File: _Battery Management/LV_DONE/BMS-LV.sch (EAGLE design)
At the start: 120 parts, among them J1 M1x5, J2 M1x4, J3 M1x4, J4 M1x4, J5 M1x2, J6 MX150L, J7 M2770166, J8 M1x5, J9 M80022232081-2, K1 ADJ14024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

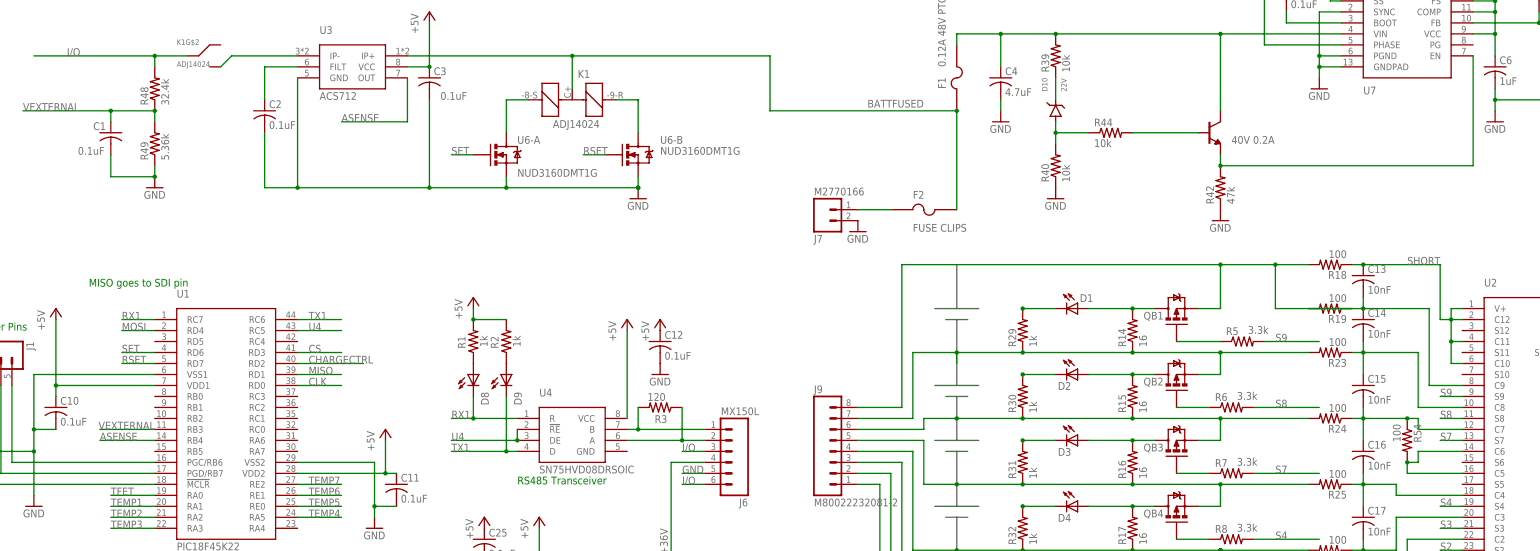
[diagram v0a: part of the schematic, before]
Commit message: 
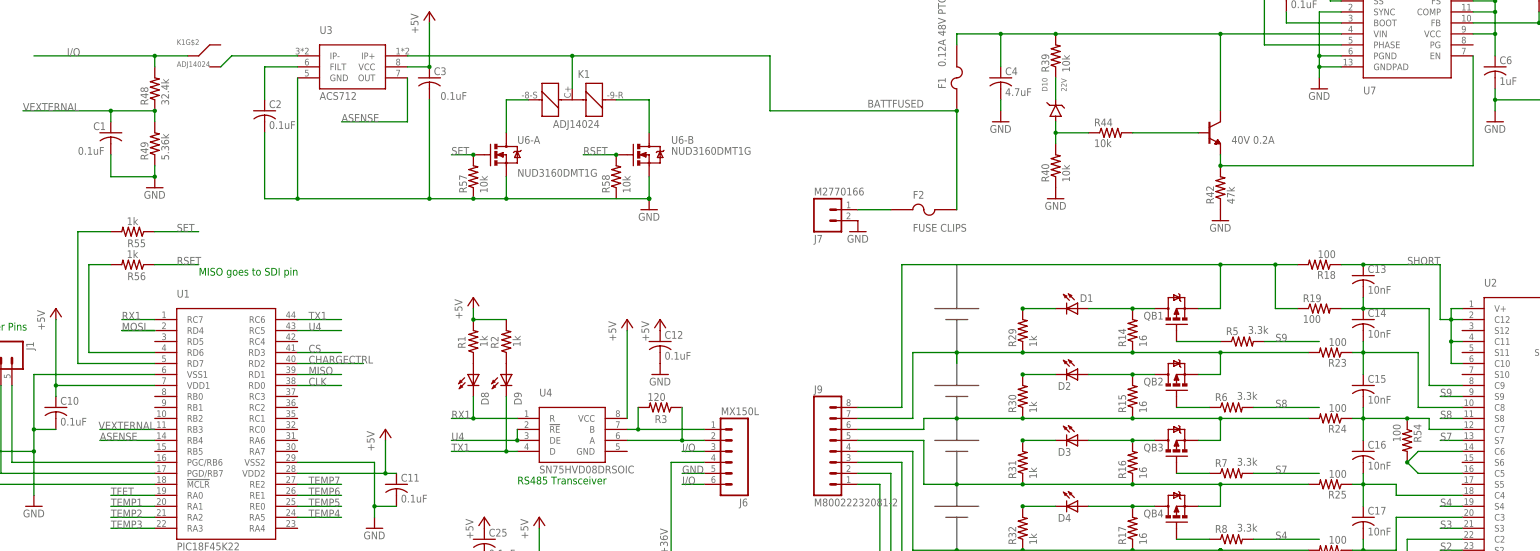
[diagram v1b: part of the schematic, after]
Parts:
- added R55, R56: 1k, FSAE Electric:RES_1K_5%
- added R57, R58: 10k, FSAE Electric:RES_10K_1%
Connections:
- new net N$19: R56.2, U1.RD6
- new net N$6: R55.2, U1.RD7
- net GND: now also R57.1
- net RSET: now also R58.2; no longer U1.RD7
- net SET: now also R55.1, R57.2; no longer U1.RD6
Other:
- moved on the sheet: R18, R19, U6-B

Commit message: 
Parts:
- removed C24: 10uF, FSAE Electric:CAP_10UF_50V
- removed C25, C26: 0.1uF, FSAE Electric:CAP_0.1UF_50V
- removed Q3: BDX34C, FSAE Electric:PNP_BDX34C
- removed R36: 1k, FSAE Electric:RES_1K_5%
- removed R38: 0.5, FSAE Electric:RES_0.5_5%_CHASSISMNT
- removed R53: 100, FSAE Electric:RES_100_1%
- removed U9: OPA344, FSAE Electric:OPA344
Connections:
- removed net +36V: J6.4, Q3.E
- removed net CHARGECTRL: R36.1, U1.RD2
- removed net N$14: C24.+, R36.2, U9.+
- removed net N$17: Q3.B, R53.2
- removed net N$21: C26.+, R53.1, U9.O
- removed net N$23: C26.-, Q3.C, R38.2, U9.-
- removed net VREG: C23.+, R47.2
- net +5V: now also C23.+, R47.2; no longer C25.+, U9.V+
- net BATTFUSED: no longer R38.1
- net GND: now also J6.2; no longer C24.-, C25.-, U9.V-
- net N$29: now also J6.4; no longer J6.2
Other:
- moved on the sheet: J6

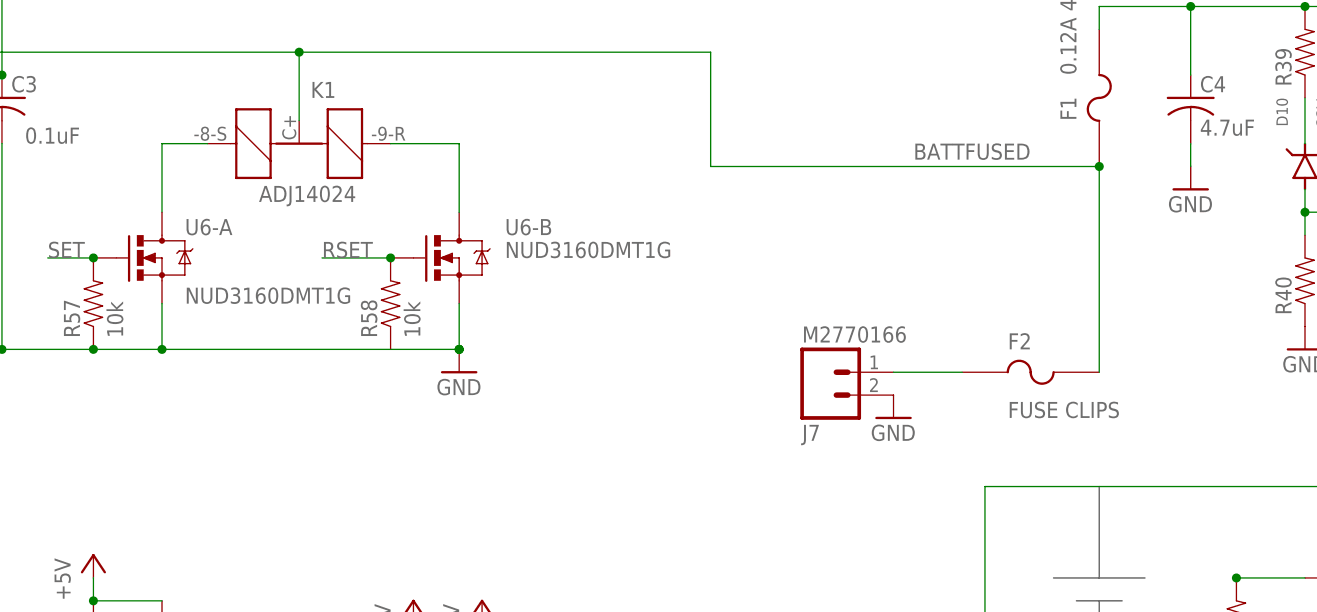
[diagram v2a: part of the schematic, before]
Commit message: 
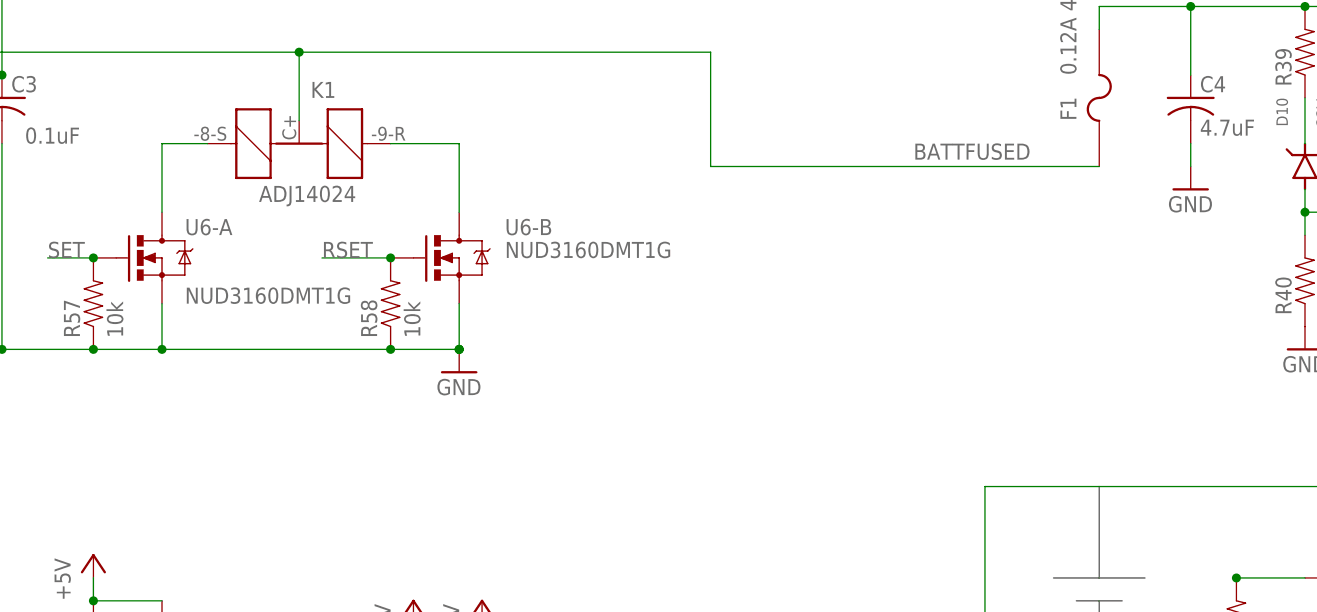
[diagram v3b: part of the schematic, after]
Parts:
- removed F2: FUSE CLIPS, FSAE Electric:FUSEFUSECLIPS
- removed J7: M2770166, FSAE Electric:M2770166
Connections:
- removed net N$5: F2.P$1, J7.1
- net BATTFUSED: no longer F2.P$2
- net GND: now also R58.1; no longer J7.2
- net RSET: now also R56.1
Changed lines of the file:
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@@
 <part name="R44" library="FSAE Electric" deviceset="RES" device="_10K_1%" value="10k"/>
 <part name="F1" library="FSAE Electric" deviceset="FUSE" device="_0.12A_48V_PTC" value="0.12A 48V PTC"/>
-<part name="F2" library="FSAE Electric" deviceset="FUSE" device="FUSECLIPS" value="FUSE CLIPS"/>
 <part name="J2" library="FSAE Electric" deviceset="M4" device="_1X4_LOCK" value="M1x4"/>
 <part name="J3" library="FSAE Electric" deviceset="M4" device="_1X4_LOCK" value="M1x4"/>
@@
 <part name="P+11" library="supply1" deviceset="+5V" device=""/>
 <part name="P+12" library="supply1" deviceset="+5V" device=""/>
-<part name="J7" library="FSAE Electric" deviceset="M2" device="770166"/>
-<part name="GND21" library="supply1" deviceset="GND" device=""/>
 <part name="FRAME1" library="frames" deviceset="DOCFIELD" device=""/>
 <part name="R54" library="FSAE Electric" deviceset="RES" device="_1K_1%_0805" value="100"/>
@@
 <attribute name="VALUE" x="256.54" y="264.16" size="1.778" layer="96" rot="R90"/>
 </instance>
-<instance part="F2" gate="G$1" x="251.46" y="231.14"/>
 <instance part="J2" gate="G$1" x="22.86" y="91.44"/>
 <instance part="J3" gate="G$1" x="22.86" y="68.58"/>
@@
 <attribute name="VALUE" x="459.74" y="198.12" size="1.778" layer="96" rot="R90"/>
 </instance>
-<instance part="J7" gate="G$1" x="231.14" y="228.6" rot="MR180"/>
-<instance part="GND21" gate="1" x="236.22" y="226.06"/>
 <instance part="FRAME1" gate="G$1" x="424.18" y="7.62" smashed="yes">
 <attribute name="SHEET" x="510.54" y="8.89" size="2.54" layer="94"/>
@@
 <wire x1="137.16" y1="233.68" x2="147.32" y2="233.68" width="0.1524" layer="91"/>
 <wire x1="147.32" y1="233.68" x2="154.94" y2="233.68" width="0.1524" layer="91"/>
-<wire x1="154.94" y1="233.68" x2="187.96" y2="233.68" width="0.1524" layer="91"/>
+<wire x1="154.94" y1="233.68" x2="180.34" y2="233.68" width="0.1524" layer="91"/>
+<wire x1="180.34" y1="233.68" x2="187.96" y2="233.68" width="0.1524" layer="91"/>
 <wire x1="154.94" y1="238.76" x2="154.94" y2="233.68" width="0.1524" layer="91"/>
 <wire x1="187.96" y1="238.76" x2="187.96" y2="233.68" width="0.1524" layer="91"/>
@@
 <pinref part="R57" gate="G$1" pin="1"/>
 <junction x="147.32" y="233.68"/>
+<pinref part="R58" gate="G$1" pin="1"/>
+<junction x="180.34" y="233.68"/>
 </segment>
 <segment>
@@
 </segment>
 <segment>
-<pinref part="J7" gate="G$1" pin="2"/>
-<pinref part="GND21" gate="1" pin="GND"/>
-</segment>
-<segment>
 <pinref part="J6" gate="G$1" pin="2"/>
 <wire x1="205.74" y1="177.8" x2="200.66" y2="177.8" width="0.1524" layer="91"/>
@@
 <wire x1="83.82" y1="218.44" x2="73.66" y2="218.44" width="0.1524" layer="91"/>
 <label x="78.74" y="218.44" size="1.778" layer="95"/>
+<pinref part="R56" gate="G$1" pin="1"/>
 </segment>
 </net>
@@
 <junction x="170.18" y="266.7"/>
 <wire x1="170.18" y1="266.7" x2="132.08" y2="266.7" width="0.1524" layer="91"/>
-<pinref part="F2" gate="G$1" pin="P$2"/>
-<wire x1="259.08" y1="231.14" x2="259.08" y2="254" width="0.1524" layer="91"/>
-<junction x="259.08" y="254"/>
 <pinref part="U3" gate="G$1" pin="IP+"/>
 <label x="251.46" y="256.54" size="1.778" layer="95" rot="R180"/>
@@
 </segment>
 </net>
-<net name="N$5" class="0">
-<segment>
-<pinref part="J7" gate="G$1" pin="1"/>
-<wire x1="236.22" y1="231.14" x2="243.84" y2="231.14" width="0.1524" layer="91"/>
-<pinref part="F2" gate="G$1" pin="P$1"/>
-</segment>
-</net>
